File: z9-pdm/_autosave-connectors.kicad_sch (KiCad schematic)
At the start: 11 parts, among them J10 Wago 12 pin 1 level 3.5mm 260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, J11 TE_DT15-12PC-B016 -Conn_01x12, J12 Wago 12 pin 1 level 3.5mm 260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, J13 TE_DT15-12PC-B016 -Conn_01x12, J14 Wago 12 pin 1 level 3.5mm 260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, J15 TE_DT15-12PC-B016 -Conn_01x12, J5 BM06B-GHS-GB-TBT(LF)(SN)(N), J6 Wago 12 pin 1 level 3.5mm 260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, J7 TE_DT15-12PC-B016 -Conn_01x12, J8 RedCubeTerminal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

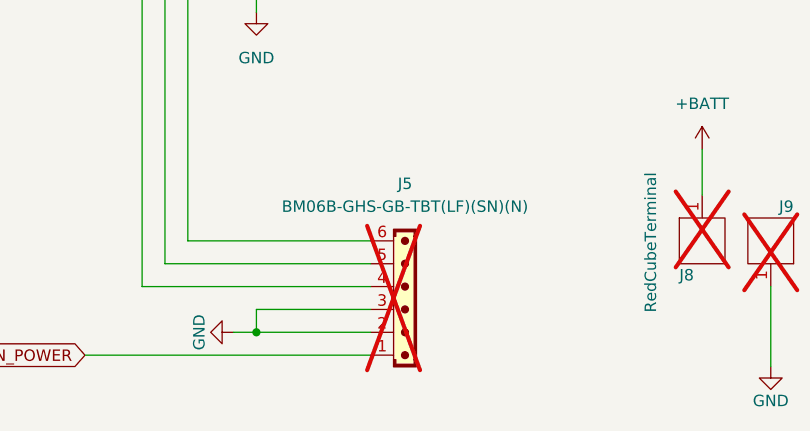
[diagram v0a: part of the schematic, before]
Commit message: fixced missing vias
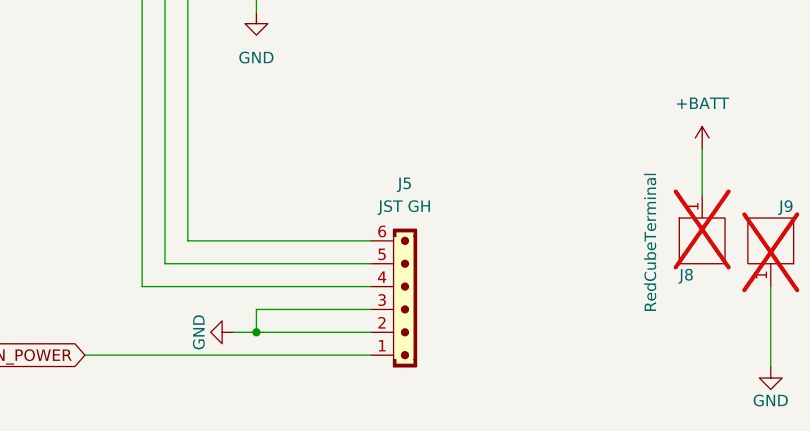
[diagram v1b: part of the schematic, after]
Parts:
- J5: value BM06B-GHS-GB-TBT(LF)(SN)(N) -> JST GH; LCSC C17467557 -> C160392; now fitted
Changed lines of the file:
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@@
 		(in_bom no)
 		(on_board yes)
-		(dnp yes)
+		(dnp no)
 		(fields_autoplaced yes)
 		(property "Reference" "J5"
@@
 			)
 		)
-		(property "Value" "BM06B-GHS-GB-TBT(LF)(SN)(N)"
+		(property "Value" "JST  GH"
 			(at 67.31 157.48 0)
 			(effects
@@
 			)
 		)
-		(property "Datasheet" ""
+		(property "Datasheet" "https://wmsc.lcsc.com/wmsc/upload/file/pdf/v2/lcsc/2304140030_JST-BM06B-GHS-TBT-LF-SN_C189892.pdf"
 			(at 67.31 179.07 0)
 			(effects
@@
 			)
 		)
-		(property "Description" "-25℃~+85℃ 1 1.25mm 10.75mm 1A 1x6P 4.05mm 4.32mm 50V 6 6P Auxiliary Solder Pin GH Gold PA9T Phosphor Bronze Surface Mount,Vertical UL94V-0 White SMD,P=1.25mm Wire To Board Connector ROHS"
+		(property "Description" "JST Connector  6 pins"
 			(at 68.072 150.368 0)
 			(effects
@@
 			)
 		)
-		(property "LCSC" "C17467557"
+		(property "LCSC" "C160392"
 			(at 67.31 177.038 0)
 			(effects
